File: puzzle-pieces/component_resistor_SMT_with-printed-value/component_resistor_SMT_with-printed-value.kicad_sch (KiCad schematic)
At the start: 11 parts, among them J1 Conn_01x02_Pin, J2 Conn_01x02_Pin

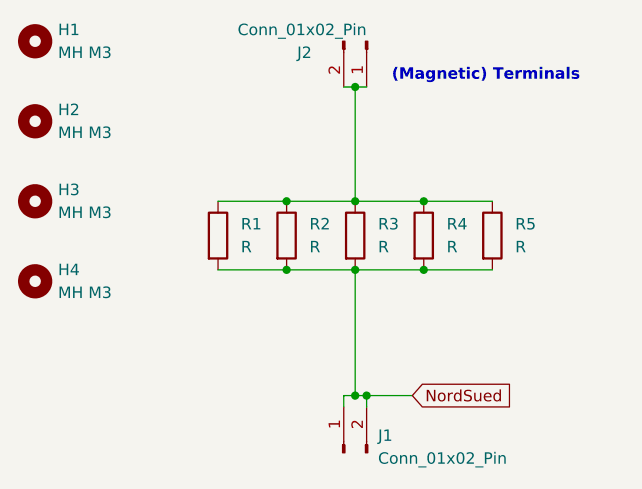
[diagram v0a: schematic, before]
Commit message: Update resistor footprints and add THT 3W production files
Replaced mounting hole footprints with SMD resistor footprints in the SMT E-6 series panel and updated net assignments. Added new KiCad PCB, project, and production ZIP files for the THT 3W E-6 series resistors. Updated connector reference and position in the SMT panel.
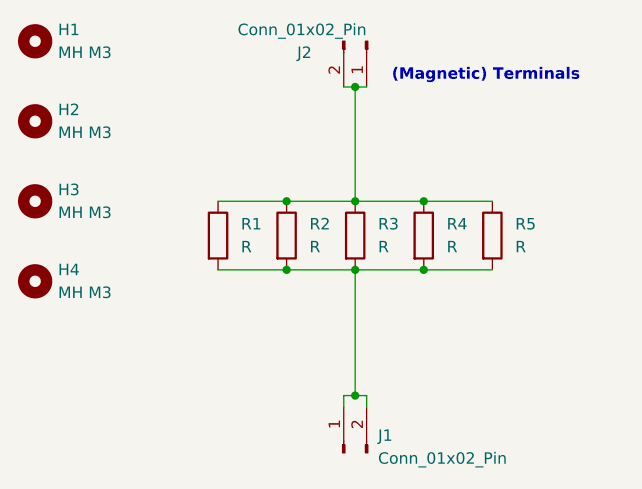
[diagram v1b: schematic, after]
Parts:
- H1, H2, H3, H4: footprint MountingHole:MountingHole_3.2mm_M3 -> EASYEDA2KICAD:MountingHole_3.0mm_M3_tight
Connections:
- net NordSued: no longer names the net of J1.1 (Pin_1), J1.2 (Pin_2), R1.2, R2.2, R3.2, R4.2, R5.2
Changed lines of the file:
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@@
-	)
-	(junction
-		(at 52.07 54.61)
-		(diameter 0)
-		(color 0 0 0 0)
 	)
 	(junction
@@
 	(wire
 		(pts
-			(xy 52.07 54.61) (xy 57.15 54.61)
-		)
-		(stroke
-			(width 0)
-			(type default)
-		)
-	)
-	(wire
-		(pts
 			(xy 50.8 20.32) (xy 52.07 20.32)
 		)
@@
 			(width 0)
 			(type default)
-		)
-	)
-	(global_label "NordSued"
-		(shape input)
-		(at 57.15 54.61 0)
-		(fields_autoplaced yes)
-		(effects
-			(font
-				(size 1.27 1.27)
-			)
-			(justify left)
-		)
-		(property "Intersheetrefs" "${INTERSHEET_REFS}"
-			(at 69.146 54.61 0)
-			(effects
-				(font
-					(size 1.27 1.27)
-				)
-				(justify left)
-				(hide yes)
-			)
 		)
 	)
@@
 			)
 		)
-		(property "Footprint" "MountingHole:MountingHole_3.2mm_M3"
+		(property "Footprint" "EASYEDA2KICAD:MountingHole_3.0mm_M3_tight"
 			(at 15.24 41.91 0)
 			(effects
@@
 			)
 		)
-		(property "Footprint" "MountingHole:MountingHole_3.2mm_M3"
+		(property "Footprint" "EASYEDA2KICAD:MountingHole_3.0mm_M3_tight"
 			(at 15.24 15.24 0)
 			(effects
@@
 			)
 		)
-		(property "Footprint" "MountingHole:MountingHole_3.2mm_M3"
+		(property "Footprint" "EASYEDA2KICAD:MountingHole_3.0mm_M3_tight"
 			(at 15.24 24.13 0)
 			(effects
@@
 			)
 		)
-		(property "Footprint" "MountingHole:MountingHole_3.2mm_M3"
+		(property "Footprint" "EASYEDA2KICAD:MountingHole_3.0mm_M3_tight"
 			(at 15.24 33.02 0)
 			(effects
